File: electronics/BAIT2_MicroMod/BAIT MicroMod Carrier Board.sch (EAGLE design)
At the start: 113 parts, among them J1 JTAG, J11 microSD, J2 JTAG, J3 QWIIC_RIGHT_ANGLE, J4 JST_6_PIN_VERTICAL, J6 MICROMOD-2222-C, U1 3.3V, U2 S-1172B33-E6T1U, U3 LoRa-E5-HF, U5 3.3V, U6 BQ27441-G1, X1 2.1mm DC, X2 BQ24074

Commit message: Schematic V1 complete
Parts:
- added E5_EXTRA_PINS: (no value), SparkFun-Connectors:CONN_15
- added MICROMOD_EXTRA_PINS: (no value), SparkFun-Connectors:CONN_08"
- added POWER_PINS: (no value), SparkFun-Connectors:CONN_05
- added XB_EXTRA_PINS: (no value), SparkFun-Connectors:CONN_02
- C16: device SparkFun-Capacitors:1.0UF-16V-10%(0603) -> SparkFun-Capacitors:1.0UF-0603-16V-10%
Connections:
- removed net N$12: R1.1
- removed net N$23: U$7.DO8
- removed net N$24: U$7.RESET
- removed net N$26: U$7.PWM1
- removed net N$27: U$7.RESERVED
- removed net N$29: U$7.DTR/DI8
- removed net N$30: U$7.AD4/DIO4
- removed net N$31: U$7.CTS/DIO7
- removed net N$32: U$7.ON/SLEEP
- removed net N$33: U$7.VREF
- removed net N$35: U$7.RTS/AD6/DIO6
- removed net N$36: U$7.AD3/DIO3
- removed net N$37: U$7.AD2/DIO2
- removed net N$38: U$7.AD1/DIO1
- removed net N$39: U$7.AD0/DIO0
- removed net SCL: U6.SCL
- removed net SDA: U6.SDA
- removed net VLIPO: BATT1.2, C16.1, C2.1, C3.1, R24.2, U6.BAT, U6.SRP
- new net XB_ON: U$7.ON/SLEEP, XB_EXTRA_PINS.1
- new net XB_RST: U$7.RESET, XB_EXTRA_PINS.2
- net 3.3V: now also POWER_PINS.2
- net 3.3V_EN: now also MICROMOD_EXTRA_PINS.1
- net A0: now also MICROMOD_EXTRA_PINS.7
- net A1: now also MICROMOD_EXTRA_PINS.6
- net D0: now also MICROMOD_EXTRA_PINS.4
- net D1: now also MICROMOD_EXTRA_PINS.3
- net GND: now also POWER_PINS.1
- net HEADER_!CS!: now also MICROMOD_EXTRA_PINS.2
- net I2C_!INT!: now also MICROMOD_EXTRA_PINS.8
- net I2C_SCL: now also U6.SCL
- net I2C_SDA: now also U6.SDA
- net PA0/D0: now also E5_EXTRA_PINS.1
- net PA10/MOSI: now also E5_EXTRA_PINS.5
- net PA2/TX2: now also E5_EXTRA_PINS.13
- net PA3/RX2: now also E5_EXTRA_PINS.12
- net PA9/D9: now also E5_EXTRA_PINS.15
- net PB10/D10: now also E5_EXTRA_PINS.14
- net PB13/BOOT/SCK: now also E5_EXTRA_PINS.2
- net PB14/MISO: now also E5_EXTRA_PINS.4
- net PB3/A3: now also E5_EXTRA_PINS.6
- net PB4/A4: now also E5_EXTRA_PINS.7
- net PB5/LED: now also E5_EXTRA_PINS.8
- net PB9/NSS: now also E5_EXTRA_PINS.3
- net PC0/RX1: now also E5_EXTRA_PINS.10
- net PC1/TX1: now also E5_EXTRA_PINS.9
- net PWM0: now also R1.1
- net PWM1: now also MICROMOD_EXTRA_PINS.5
- net RST: now also E5_EXTRA_PINS.11
- net V+: now also POWER_PINS.4
- net VBUS: now also POWER_PINS.5
- net VIN: now also BATT1.2, C16.1, C2.1, C3.1, R24.2, U6.BAT, U6.SRP
- net V_BATT: now also POWER_PINS.3
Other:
- note added: "Headers"
- moved on the sheet: C17

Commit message: Initial board layout
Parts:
- removed 3V3_LED1, IN_LED, IN_LED1, OUT_LED, OUT_LED1, VIN_LED1: JUMPER-SMT_2_NC_TRACE_SILK, SparkFun-Jumpers:JUMPER-SMT_2_NC_TRACE_SILK
- removed BATT1: JST 2PH, adafruit:JST_2PIN-SMT-RA
- removed BT1: ML414H, SparkFun-Batteries:ML414H_IV01E_BATTERY
- removed C1, C16, C19: 1.0uF, SparkFun-Capacitors:1.0UF-0603-16V-10%
- removed C17: 0.47uF, SparkFun-Capacitors:CAP0603-CAP
- removed C18: 10uF, SparkFun-Capacitors:10UF-POLAR-EIA3216-16V-10%(TANT)
- removed C2: 10uF, microbuilder:CAP_CERAMIC0805-NOOUTLINE
- removed C20, C46, C9: 0.1uF, SparkFun-Capacitors:0.1UF-0603-25V-(+80/-20%)
- removed C21, C8: 0.22uF, SparkFun-Capacitors:0.22UF-0603-25V-10%
- removed D11, D3: GREEN, SparkFun-LED:LED-GREEN0603
- removed D13, D14, D5: RED, SparkFun-LED:LED-RED0603
- removed D2: BAS70-05, SparkFun-DiscreteSemi:DIODE-SCHOTTKY-DUAL
- removed D6: 3A/10V/280mV, SparkFun-DiscreteSemi:DIODE-SCHOTTKY-BAT60A
- removed D7: RED, microbuilder:LED0603
- removed D8: SK34A, microbuilder:DIODE-SCHOTTKYSMA
- removed D9: Yellow, SparkFun-LED:LED-YELLOW0603
- removed J11: microSD, SparkFun-Connectors:MICRO-SD-SDIOPUSH-PUSH
- removed J3: QWIIC_RIGHT_ANGLE, SparkFun-Connectors:QWIIC_CONNECTORJS-1MM
- removed J7: (no value), SparkFun-Connectors:CONN_02-JST-2MM-SMT
- removed JP2, JP4, JP6, JP7, JP8, JP9: JUMPER-SMT_3_1-NC_TRACE_SILK, SparkFun-Jumpers:JUMPER-SMT_3_1-NC_TRACE_SILK
- removed JP3: (no value), microbuilder:HEADER-1X1
- removed MEAS1: JUMPER-COMBO_2_NC_TRACE, SparkFun-Jumpers:JUMPER-COMBO_2_NC_TRACE
- removed R11, R19, R2, R6, R7: 1k, SparkFun-Resistors:1KOHM-0603-1/10W-1%
- removed R18: 590, microbuilder:RESISTOR_0603_NOOUT
- removed R20: 1K, microbuilder:RESISTOR_0603_NOOUT
- removed R22: 2.2k, SparkFun-Resistors:2.2KOHM-0603-1/10W-1%
- removed R25: 4.7k, SparkFun-Resistors:4.7KOHM-0603-1/10W-1%
- removed R26: 100k, SparkFun-Resistors:100KOHM-0603-1/10W-1%
- removed R27, R28, R29, R30: 10K, microbuilder:RESISTOR_0603_NOOUT
- removed R5: 3.3k, SparkFun-Resistors:3.3KOHM-0603-1/10W-1%
- removed THERM1: JUMPER-SMT_2_NO_NO-SILK, SparkFun-Jumpers:JUMPER-SMT_2_NO_NO-SILK
- removed U1: 3.3V, SparkFun-IC-Power:V_REG_AP2112K-3.3V
- removed U2: S-1172B33-E6T1U, Ablic:S-1172B33-E6T1U
- removed U6: BQ27441-G1, SparkFun-PowerIC:BQ27441-G1
- added 3V3_LED2, J_RX, J_TX, VIN_LED2: JUMPER-SMT_2_NC_TRACE_SILK, SparkFun-Jumpers:JUMPER-SMT_2_NC_TRACE_SILK
- added BATT2: JST 2PH, adafruit:JST_2PIN-SMT-RA
- added BT3: ML414H, SparkFun-Batteries:ML414H_IV01E_BATTERY
- added C13, C14, C28: 1.0uF, SparkFun-Capacitors:1.0UF-0603-16V-10%
- added C22: 10uF, microbuilder:CAP_CERAMIC0805-NOOUTLINE
- added C25, C30: 0.22uF, SparkFun-Capacitors:0.22UF-0603-25V-10%
- added C26, C29, C6: 0.1uF, SparkFun-Capacitors:0.1UF-0603-25V-(+80/-20%)
- added C27: 10uF, SparkFun-Capacitors:10UF-POLAR-EIA3216-16V-10%(TANT)
- added C7: 0.47uF, SparkFun-Capacitors:CAP0603-CAP
- added D16: Yellow, SparkFun-LED:LED-YELLOW0603
- added D17: RED, microbuilder:LED0603
- added D18: 3A/10V/280mV, SparkFun-DiscreteSemi:DIODE-SCHOTTKY-BAT60A
- added D19: BAS70-05, SparkFun-DiscreteSemi:DIODE-SCHOTTKY-DUAL
- added D20: SK34A, microbuilder:DIODE-SCHOTTKYSMA
- added D21: GREEN, microbuilder:LED0603
- added D_RX: GREEN, SparkFun-LED:LED-GREEN0603
- added D_TX: RED, SparkFun-LED:LED-RED0603
- added E5_SWO: JTAG, SparkFun-Connectors:CORTEX_JTAG_DEBUG_MINIMUM_PTH
- added JP_CIPO, JP_COPI, JP_CS, JP_SCK: JUMPER-SMT_3_1-NC_TRACE_SILK, SparkFun-Jumpers:JUMPER-SMT_3_1-NC_TRACE_SILK
- added LORA-E5: LoRa-E5-HF, moudle-new:MOUDLE_LORA_E5
- added MEAS2: JUMPER-COMBO_2_NC_TRACE, SparkFun-Jumpers:JUMPER-COMBO_2_NC_TRACE
- added QWIIC_PWR: JUMPER-SMT_3_2-NC_TRACE_SILK, SparkFun-Jumpers:JUMPER-SMT_3_2-NC_TRACE_SILK
- added R32: 3.3k, SparkFun-Resistors:3.3KOHM-0603-1/10W-1%
- added R34, R35: 2.2k, SparkFun-Resistors:2.2KOHM-0603-1/10W-1%
- added R36: 100k, SparkFun-Resistors:100KOHM-0603-1/10W-1%
- added R38, R41, R42, R43, R44: 10K, microbuilder:RESISTOR_0603_NOOUT
- added R39: 590, microbuilder:RESISTOR_0603_NOOUT
- added R40: 1K, microbuilder:RESISTOR_0603_NOOUT
- added REG1: S-1172B33-E6T1U, Ablic:S-1172B33-E6T1U
- added R_RX, R_TX: 1k, SparkFun-Resistors:1KOHM-0603-1/10W-1%
- added SOLAR_JST1: (no value), SparkFun-Connectors:CONN_02-JST-2MM-SMT
- added THERM2: JUMPER-SMT_2_NO_NO-SILK, SparkFun-Jumpers:JUMPER-SMT_2_NO_NO-SILK
- added U4: 3.3V, SparkFun-IC-Power:V_REG_AP2112K-3.3V
- added USBC: (no value), SparkFun-Connectors:USB_C_2-LAYER_PADS
- C15: value 1.0uF -> 10uF; device SparkFun-Capacitors:1.0UF-0603-16V-10% -> microbuilder:CAP_CERAMIC0805-NOOUTLINE
- C3: value 10uF -> 1.0uF; device microbuilder:CAP_CERAMIC0805-NOOUTLINE -> SparkFun-Capacitors:1.0UF-16V-10%(0603)
- D10: value GREEN -> RED; device microbuilder:LED0603 -> SparkFun-LED:LED-RED0603
- J1: value JTAG -> microSD; device SparkFun-Connectors:CORTEX_JTAG_DEBUG_MINIMUM_PTH -> SparkFun-Connectors:MICRO-SD-SDIOPUSH-PUSH
- J5: value (none) -> QWIIC_RIGHT_ANGLE; device SparkFun-Connectors:USB_C_2-LAYER_PADS -> SparkFun-Connectors:QWIIC_CONNECTORJS-1MM
- JP1: value JUMPER-SMT_3_2-NC_TRACE_SILK -> (none); device SparkFun-Jumpers:JUMPER-SMT_3_2-NC_TRACE_SILK -> microbuilder:HEADER-1X1
- R17: value 10K -> 0.01; device microbuilder:RESISTOR_0603_NOOUT -> SparkFun-Resistors:RESISTOR1206; PROD_ID (none) -> RES-13218
- R21: value 2.2k -> 100k; device SparkFun-Resistors:2.2KOHM-0603-1/10W-1% -> SparkFun-Resistors:100KOHM-0603-1/10W-1%
- R23: value 100k -> 1k; device SparkFun-Resistors:100KOHM-0603-1/10W-1% -> SparkFun-Resistors:1KOHM-0603-1/10W-1%
- R24: value 0.01 -> 4.7k; device SparkFun-Resistors:RESISTOR1206 -> SparkFun-Resistors:4.7KOHM-0603-1/10W-1%; PROD_ID RES-13218 -> (none)
- U3: value LoRa-E5-HF -> 3.3V; device moudle-new:MOUDLE_LORA_E5 -> SparkFun-IC-Power:V_REG_AP2112K-3.3V
- U5: value 3.3V -> BQ27441-G1; device SparkFun-IC-Power:V_REG_AP2112K-3.3V -> SparkFun-PowerIC:BQ27441-G1; PROD_ID (none) -> IC-13220
- renumbered ASC_LED to J_ASC, D12 to D_RSSI\, D4 to D_ASC, J2 to MM_SWO, J6 to MICROMOD, R4 to R_ASC, R8 to R_RSSI, RSSI_LED to J_RSSI, U$7 to XBEE
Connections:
- removed net N$11: R28.1, THERM1.1
- removed net N$14: BT1.+, D6.A, R5.1
- removed net N$15: JP1.3, R22.2
- removed net N$17: MEAS1.1, U2.VOUT
- removed net N$18: 3V3_LED1.1, R6.2
- removed net N$20: D5.A, R6.1
- removed net N$21: R25.2, VIN_LED1.1
- removed net N$22: D9.A, R25.1
- removed net N$40: IN_LED.1, R7.2
- removed net N$41: D11.A, R7.1
- removed net N$46: OUT_LED.1, R19.2
- removed net N$47: D14.A, R19.1
- removed net N$7: D7.C, R17.2
- removed net N$8: D10.C, R29.2
- removed net XB_IN: JP9.3, XBEE.DIN
- removed net XB_OUT: JP8.3, XBEE.DOUT
- new net GND1: SOLAR_JST1.2, X1.GND, X1.GNDBREAK
- new net N$23: BT3.+, D18.A, R32.1
- new net N$24: QWIIC_PWR.3, R35.2
- new net N$26: QWIIC_PWR.1, R34.2
- new net N$27: D10.A, R23.1
- new net N$29: R24.2, VIN_LED2.1
- new net N$30: D20.A, SOLAR_JST1.1, X1.PWR
- new net N$31: D17.C, R38.2
- new net N$32: D21.C, R43.2
- new net N$33: R42.1, THERM2.1
- new net N$37: D16.A, R24.1
- new net OUT: X2.EN2
- new net V+1: REG1.VIN
- net !CE: now also R44.1; no longer R30.1
- net !CHG: now also R38.1; no longer R17.1
- net !PGOOD: now also R43.1; no longer R29.1
- net 1.8V: now also C7.1, U5.VDD; no longer C17.1, U6.VDD
- net 3.3V: now also 3V3_LED2.2, C28.1, C29.1, C30.1, D19.A1, E5_SWO.VCC, J_RX.2, J_TX.2, LORA-E5.VCC, MEAS2.2, R21.2, R36.2; no longer 3V3_LED1.2, C19.1, C20.1, C21.1, D2.A1, IN_LED.2, IN_LED1.2, J1.VCC, MEAS1.2, OUT_LED.2, OUT_LED1.2, R23.2, R26.2, U3.VCC
- net 3.3V_LP: now also C14.1, C6.1, J1.VCC, U4.OUT; no longer C1.1, C46.1, J11.VCC, U1.OUT
- net CLK/SCK: now also J1.CLK/SCK, JP_SCK.3; no longer J11.CLK/SCK, JP6.3
- net CMD/CIPO: now also J1.CMD/SDI, JP_CIPO.3; no longer J11.CMD/SDI, JP7.3
- net DAT0/COPI: now also J1.DAT0/SDO, JP_COPI.3; no longer J11.DAT0/SDO, JP4.3
- net DAT3/!CS!: now also J1.DAT3/!CS!, JP_CS.3; no longer J11.DAT3/!CS!, JP2.3
- net GND: now also BATT2.1, BT3.-, C13.2, C14.2, C22.2, C25.2, C26.2, C27.-, C28.2, C29.2, C30.2, C6.2, C7.2, D10.C, D16.C, E5_SWO.GND, J1.SHIELD, J5.1, JP1.1, LORA-E5.GND, LORA-E5.GND@1, LORA-E5.GND@2, LORA-E5.GND@3, R39.2, R40.2, R41.2, R42.2, R44.2, REG1.VSS, REG1.VSS_2, U4.GND, U5.PWPD, U5.VSS, USBC.GND; no longer BATT1.1, BT1.-, C1.2, C16.2, C17.2, C18.-, C19.2, C2.2, C20.2, C21.2, C46.2, C8.2, C9.2, D5.C, D9.C, J11.GND, J11.SHIELD, J3.1, J5.GND, J7.2, JP3.1, R18.2, R20.2, R27.2, R28.2, R30.2, U1.GND, U2.VSS, U2.VSS_2, U3.GND@1, U3.GND@2, U3.GND@3, U5.GND, U6.PWPD, U6.VSS, X1.GND, X1.GNDBREAK
- net GPOUT: now also U5.GPOUT; no longer U6.GPOUT
- net I2C_SCL: now also J5.4, R35.1, U5.SCL; no longer J3.4, R22.1, U6.SCL
- net I2C_SDA: now also J5.3, R34.1, U5.SDA; no longer J3.3, R21.1, U6.SDA
- net ILIM: now also R40.1; no longer R20.1
- net ISET: now also R39.1; no longer R18.1
- net ITERM: now also R41.1; no longer R27.1
- net N$16: now also 3V3_LED2.1, R23.2; no longer JP1.1, R21.2
- net N$19: now also LORA-E5.VDD_TCXO; no longer U3.VDD_TCXO
- net N$3: now also J_RX.1, R_RX.2; no longer IN_LED1.1, R2.2
- net N$4: now also USBC.CC1; no longer J5.CC1
- net N$44: now also J_TX.1, R_TX.2; no longer OUT_LED1.1, R11.2
- net N$45: now also D_TX.A, R_TX.1; no longer D13.A, R11.1
- net N$48: now also USBC.VBUS; no longer J5.VBUS
- net N$5: now also USBC.CC2; no longer J5.CC2
- net N$6: now also MEAS2.1, REG1.VOUT; no longer D8.A, J7.1, X1.PWR
- net N$9: now also D_RX.A, R_RX.1; no longer D3.A, R2.1
- net PA0/D0: now also LORA-E5.PA0; no longer U3.PA0
- net PA10/MOSI: now also LORA-E5.PA10; no longer U3.PA10
- net PA13/SWDIO: now also E5_SWO.SWDIO, LORA-E5.PA13; no longer J1.SWDIO, U3.PA13
- net PA14/SWCLK: now also E5_SWO.SWDCLK, LORA-E5.PA14; no longer J1.SWDCLK, U3.PA14
- net PA15/SDA: now also LORA-E5.PA15; no longer U3.PA15
- net PA2/TX2: now also LORA-E5.PA2; no longer U3.PA2
- net PA3/RX2: now also LORA-E5.PA3; no longer U3.PA3
- net PA9/D9: now also LORA-E5.PA9; no longer U3.PA9
- net PB10/D10: now also LORA-E5.PB10; no longer U3.PB10
- net PB13/BOOT/SCK: now also LORA-E5.PB13; no longer U3.PB13
- net PB14/MISO: now also LORA-E5.PB14; no longer U3.PB14
- net PB15/SCL: now also LORA-E5.PB15; no longer U3.PB15
- net PB3/A3: now also LORA-E5.PB3; no longer U3.PB3
- net PB4/A4: now also LORA-E5.PB4; no longer U3.PB4
- net PB5/LED: now also LORA-E5.PB5; no longer U3.PB5
- net PB9/NSS: now also LORA-E5.PB9; no longer U3.PB9
- net PC0/RX1: now also LORA-E5.PC0; no longer U3.PC0
- net PC1/TX1: now also LORA-E5.PC1; no longer U3.PC1
- net PERIPHERAL_PWR_CTRL: now also R21.1, U4.EN; no longer R26.1, U1.EN
- net QWIIC_PWR: now also C13.1, J5.2, QWIIC_PWR.2, U3.OUT; no longer C15.1, J3.2, JP1.2, U5.OUT
- net QWIIC_PWR_CTRL: now also R36.1, U3.EN; no longer R23.1, U5.EN
- net RF: now also LORA-E5.RFI0; no longer U3.RFI0
- net RST: now also E5_SWO.!RESET, LORA-E5.RST; no longer J1.!RESET, U3.RST
- net RTC_3V: now also D18.C, D19.C, R32.2; no longer D2.C, D6.C, R5.2
- net RX: now also D_RX.C, LORA-E5.PB7, XBEE.DOUT; no longer D3.C, JP8.2, U3.PB7
- net RX2: no longer D11.C, JP8.1
- net SD_!CS!: now also JP_CS.1; no longer JP2.1
- net SD_CLK: now also JP_SCK.2; no longer JP6.2
- net SD_CMD: now also JP_CIPO.2; no longer JP7.2
- net SD_DATA0: now also JP_COPI.2; no longer JP4.2
- net SD_DATA1: now also J1.DAT1/NC; no longer J11.DAT1/NC
- net SD_DATA2: now also J1.DAT2/NC; no longer J11.DAT2/NC
- net SD_DATA3: now also JP_CS.2; no longer JP2.2
- net SPI_CIPO: now also JP_CIPO.1; no longer JP7.1
- net SPI_COPI: now also JP_COPI.1; no longer JP4.1
- net SPI_SCK: now also JP_SCK.1; no longer JP6.1
- net THERM: now also THERM2.2; no longer THERM1.2
- net TS: now also U5.BIN; no longer U6.BIN
- net TX: now also D_TX.C, LORA-E5.PB6, XBEE.DIN; no longer D13.C, JP9.2, U3.PB6
- net TX2: no longer D14.C, JP9.1
- net USB_D+: now also USBC.D+; no longer J5.D+
- net USB_D-: now also USBC.D-; no longer J5.D-
- net V+: now also C25.1, C26.1, C27.+, D17.A, D21.A, U3.IN, U4.IN, VIN_LED2.2; no longer C18.+, C8.1, C9.1, D10.A, D7.A, U1.IN, U2.VIN, VIN_LED1.2, X2.EN2
- net VBUS: now also D20.C; no longer D8.C
- net VIN: now also BATT2.2, C15.1, C22.1, R17.2, U5.BAT, U5.SRP; no longer BATT1.2, C16.1, C2.1, R24.2, U5.IN, U6.BAT, U6.SRP
- net V_BATT: now also R17.1, U5.SRN; no longer R24.1, U6.SRN
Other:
- note added: "Close VE to enable processor control of 3.3V bus."
- note removed: "BQ27441-G1 Fuel Gauge"
- note removed: "Closing jumper bypasses PTC to allow >2A current flows."
- note removed: "External Capacitor"
- note removed: "LiPo Solar Charger"
- note removed: "Peripheral Power Control"
- note removed: "Qwiic"
- note removed: "RTC"
- note removed: "USB"
- note removed: "Voltage Regulation"

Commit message: Board layout updates
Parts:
- removed ANT1: DIP SMA-K, Connector-new:ANTENNA-SMA-MCX-JE-320160125
- removed R16: DNP, Discrete-new:RES-0402
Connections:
- removed net N$10: ANT2.D, R16.2
- removed net N$13: ANT1.ANT, R15.2
- new net N$7: ANT2.D, R15.2
- net GND: no longer ANT1.2, ANT1.3, ANT1.4, ANT1.5
- net N$28: no longer R16.1
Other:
- moved on the sheet: ANT2, C11, C12, R14, R15

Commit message: Files for First Prototype production
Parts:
- removed 3V3_LED2: JUMPER-SMT_2_NC_TRACE_SILK, SparkFun-Jumpers:JUMPER-SMT_2_NC_TRACE_SILK
- removed BATT2: JST 2PH, adafruit:JST_2PIN-SMT-RA
- removed BT3: ML414H, SparkFun-Batteries:ML414H_IV01E_BATTERY
- removed D_ASC, D_RSSI\, D_RX: GREEN, SparkFun-LED:LED-GREEN0603
- removed D_TX: RED, SparkFun-LED:LED-RED0603
- removed LORA-E5: LoRa-E5-HF, moudle-new:MOUDLE_LORA_E5
- removed MICROMOD: MICROMOD-2222-C, SparkFun-MicroMod:MICROMOD-2222-C
- removed REG1: S-1172B33-E6T1U, Ablic:S-1172B33-E6T1U
- removed R_ASC: 4.7k, SparkFun-Resistors:4.7KOHM-0603-1/10W-1%
- removed R_RSSI, R_RX, R_TX: 1k, SparkFun-Resistors:1KOHM-0603-1/10W-1%
- removed S1: Reset, SparkFun-Switches:MOMENTARY-SWITCH-SPST-SMD-5.2-TALL-REDUNDANT
- removed S2: BOOT, SparkFun-Switches:MOMENTARY-SWITCH-SPST-SMD-5.2-TALL-REDUNDANT
- removed SOLAR_JST1: (no value), SparkFun-Connectors:CONN_02-JST-2MM-SMT
- removed USBC: (no value), SparkFun-Connectors:USB_C_2-LAYER_PADS
- removed X1: 2.1mm DC, microbuilder:DCBARRELSMT
- removed X2: BQ24074, adafruit_power:BQ24074
- removed XBEE: XBEE, adafruit:XBEE
- added 3V3_LED, GND_CON: JUMPER-SMT_2_NC_TRACE_SILK, SparkFun-Jumpers:JUMPER-SMT_2_NC_TRACE_SILK
- added ANT1: 0868AT43A0020EANT_0868AT43A0020E_JOT, 2023-01-04_20-35-52_Library:0868AT43A0020EANT_0868AT43A0020E_JOT
- added BT1: ML414H, SparkFun-Batteries:ML414H_IV01E_BATTERY
- added C1, C17, C19, C20, C21, C23, C31, C8: 2.2uF, SparkFun-Capacitors:10UF-POLAR-0603-6.3V-20%(TANT)
- added C16, C2, C24, C9: 0.1uF, SparkFun-Capacitors:10UF-POLAR-EIA3216-16V-10%(TANT)
- added C18: 0.15uF, SparkFun-Capacitors:10UF-POLAR-EIA3216-16V-10%(TANT)
- added C32, C34, C35, C37, C38: 100nf, OPL_Capacitor:CERAMIC-100NF-50V-10%-X7R(0603)
- added C33: 4.7uF, Discrete-new:CAP-0603
- added C36: 10uf, OPL_Capacitor:TANTALUM-SMD-10UF-16V-10%(AVX-A)
- added C39: 220pF, Capacitor:C_CHIP-0603(1608-METRIC)
- added D2, D3, D4: GREEN, SparkFun-LED:LED-GREEN0603
- added D5: RED, SparkFun-LED:LED-RED0603
- added F1: 6V/2A, Circuit-Protection:FUSE_CHIP-1206(3216-METRIC)
- added FB1: 600Ω/1.8A, SparkFun-Coils:FERRITE_BEAD-0603
- added J10: QWIIC_RIGHT_ANGLE, SM04B-SRSS-TB_LF__SN_:SM04B-SRSS-TB(LF)(SN)
- added J15: SM06B-SRSS-TB(LF)(SN), SM06B-SRSS-TB_LF__SN_:SM06B-SRSS-TB(LF)(SN)
- added J2: ST-TF-003A, ST-TF-003A:ST-TF-003A
- added J3: (no value), SparkFun-RF:XBEESMD
- added J6: JST 2PH, adafruit:JST_2PIN-SMT-RA
- added J7: MICROMOD-2222-C, SparkFun-MicroMod:MICROMOD-2222-C
- added J8: (no value), SparkFun-Connectors:CONN_02-JST-2MM-SMT
- added J9: (no value), SparkFun-Connectors:USB_C_2-LAYER_PADS
- added LINEIN, LINEOUT: (no value), SparkFun-Connectors:CONN_03
- added MIC_3V3, MIC_GND: JUMPER-SMT_3_2-NC_TRACE_SILK, SparkFun-Jumpers:JUMPER-SMT_3_2-NC_TRACE_SILK
- added MK1: ICS-43432, Audio-Devices:ICS-43432
- added MK1_LR: MK1_LR, SparkFun-Jumpers:JUMPER-SMT_3_1-NC_TRACE_SILK
- added MK2: SPH0645LM4H-B, SPH0645LM4H-B:SPH0645LM4H-B
- added MK2_LR: MK2_LR, SparkFun-Jumpers:JUMPER-SMT_3_1-NC_TRACE_SILK
- added R11, R5: 4.7K, OPL_Resistor:SMD-RES-4.7K-5%-1/10W(0603)
- added R18: 100K, OPL_Resistor:SMD-RES-100K-1%-1/10W(0603)
- added R2: 2.2K, OPL_Resistor:SMD-RES-2.2K-5%-1/10W(0603)
- added R4: 0R, OPL_Resistor:SMD-RES-0R-5%-1/10W(0603)
- added R6, R7, R8: 1K 1/10W, OPL_Resistor:SMD-RES-1K-5%-1/10W(0603)
- added SW1, SW2: SKQGADE010, OPL_Switch:SMD-BUTTON(4P-5.2X5.2X1.5MM-SKQGADE010)-SKQGADE010
- added TP1, TP3: PTR1TP06R, testpad:PTR1TP06R
- added U1: SGTL5000-32, Freescale:SGTL5000-32
- added U10: TSL25911, 2023-02-07_20-42-29_Library:TSL25911FNSON-06-FN_2000X2400_AMS
- added U2: AP7313, 2022-08-05_10-01-44_Library:AP7313
- added U6: BQ24074, adafruit_power:BQ24074
- added U7: LoRa-E5-HF, moudle-new:MOUDLE_LORA_E5
- added U8: S-1172B33-E6T1U, Ablic:S-1172B33-E6T1U
- added U9: BOSCH_TOOLS_BME680BOSCH_TOOLS_BME680_0_0, Bosch Tools - BME680:BOSCH_TOOLS_BME680BOSCH_TOOLS_BME680_0_0
- C10: value 4.7uF -> 4.7uf; device Discrete-new:CAP-0603 -> OPL_Capacitor:CERAMIC-4.7UF-10V-10%-X5R(0603)
- C13, C14, C28: value 1.0uF -> 1uf; device SparkFun-Capacitors:1.0UF-0603-16V-10% -> OPL_Capacitor:CERAMIC-1UF-25V-10%-X7R(0603)
- C15, C22, C4, C5: value 10uF -> 4.7uf; device microbuilder:CAP_CERAMIC0805-NOOUTLINE -> OPL_Capacitor:CERAMIC-4.7UF-10V-10%-X5R(0603)
- C25, C30: value 0.22uF -> 220nf; device SparkFun-Capacitors:0.22UF-0603-25V-10% -> OPL_Capacitor:CERAMIC-220NF-25V-10%-X7R(0603)
- C26, C29, C6: value 0.1uF -> 100nf; device SparkFun-Capacitors:0.1UF-0603-25V-(+80/-20%) -> OPL_Capacitor:CERAMIC-100NF-50V-10%-X7R(0603)
- C27: value 10uF -> 10uf; device SparkFun-Capacitors:10UF-POLAR-EIA3216-16V-10%(TANT) -> OPL_Capacitor:TANTALUM-SMD-10UF-16V-10%(AVX-A)
- C3: value 1.0uF -> 1uf; device SparkFun-Capacitors:1.0UF-16V-10%(0603) -> OPL_Capacitor:CERAMIC-1UF-25V-10%-X7R(0603)
- C7: MPN (none) -> TACL474K010XTA
- D1: MPN (none) -> BAS16J,115
- D15, D20: MPN (none) -> SK34A-LTP
- D16: MPN (none) -> LTST-S270KSKT
- D17: device microbuilder:LED0603 -> SparkFun-LED:LED-RED0603
- D18: MPN (none) -> BAT60AE6327HTSA1
- D19: MPN (none) -> BAS70-05-7-F
- D21: device microbuilder:LED0603 -> SparkFun-LED:LED-GREEN0603
- J1: value microSD -> SJ-43516-SMT; device SparkFun-Connectors:MICRO-SD-SDIOPUSH-PUSH -> SnapEDA-Library:SJ-43516-SMT; MPN (none) -> SJ-43516-SMT
- J4: MPN (none) -> BM06B-SRSS-TB(LF)(SN)
- J5: MPN (none) -> BM04B-SRSS-TB(LF)(SN)
- LS1: MPN (none) -> 102-CMT-7525-80-SMT-TR-ND
- R1: value 180 -> 200K; device SparkFun-Resistors:180OHM-0603-1/10W-1% -> OPL_Resistor:SMD-RES-200K-5%-1/10W(0603)
- R10: value 20k -> 20K; device SparkFun-Resistors:20KOHM-0603-1/10W-1% -> OPL_Resistor:SMD-RES-20K-1%-1/10W(0603)
- R14, R15: device Discrete-new:RES-0402 -> OPL_Resistor:SMD-RES-0R-5%-1/10W(0603)
- R17: MPN (none) -> LR1206-21R010J4
- R21, R3, R36: value 100k -> 100K; device SparkFun-Resistors:100KOHM-0603-1/10W-1% -> OPL_Resistor:SMD-RES-100K-1%-1/10W(0603)
- R23: value 1k -> 1K 1/10W; device SparkFun-Resistors:1KOHM-0603-1/10W-1% -> OPL_Resistor:SMD-RES-1K-5%-1/10W(0603)
- R24: value 4.7k -> 4.7K; device SparkFun-Resistors:4.7KOHM-0603-1/10W-1% -> OPL_Resistor:SMD-RES-4.7K-5%-1/10W(0603)
- R32: value 3.3k -> 3.3K; device SparkFun-Resistors:3.3KOHM-0603-1/10W-1% -> OPL_Resistor:SMD-RES-3.3K-1%-1/10W(0603)
- R34, R35: value 2.2k -> 2.2K; device SparkFun-Resistors:2.2KOHM-0603-1/10W-1% -> OPL_Resistor:SMD-RES-2.2K-5%-1/10W(0603)
- R38, R41, R42, R43, R44: value 10K -> 10K 1/10W; device microbuilder:RESISTOR_0603_NOOUT -> OPL_Resistor:SMD-RES-10K-5%-1/10W(0603)
- R39: device microbuilder:RESISTOR_0603_NOOUT -> OPL_Resistor:SMD-RES-560R-5%-1/10W(0603); MPN (none) -> RC0603FR-07590RL
- R40: value 1K -> 1K 1/10W; device microbuilder:RESISTOR_0603_NOOUT -> OPL_Resistor:SMD-RES-1K-5%-1/10W(0603)
- R9: value 10k -> 10K 1/10W; device SparkFun-Resistors:10KOHM-0603-1/10W-1% -> OPL_Resistor:SMD-RES-10K-5%-1/10W(0603)
- TH1, TH2, TH3, TH4: device varistor:VARISTORCN0603 -> NTCG163JX103DT1S:NTCG163JX103DT1S
- TR1: MPN (none) -> MMBT2222ATPMSTR-ND
- U4: MPN (none) -> AP2112K-3.3TRG1
- U5: MPN (none) -> BQ27441DRZT-G1A
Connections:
- removed net GND1: SOLAR_JST1.2, X1.GND, X1.GNDBREAK
- removed net OUT: X2.EN2
- removed net PA15/SDA: LORA-E5.PA15
- removed net PB15/SCL: LORA-E5.PB15
- removed net RX2: MICROMOD.RX2
- removed net THERM: TH1.1, TH3.1, THERM2.2, X2.TS
- removed net TX2: MICROMOD.TX2
- removed net V+1: REG1.VIN
- removed net VCC: XBEE.VCC
- new net 3V3_B: C34.1, C35.1, J10.2, J15.1, MIC_3V3.2, MK1_LR.1, MK2_LR.3, TP1.TP, U10.VDD, U9.VDD
- new net 3V3_ICS: C37.1, MIC_3V3.3, MK1.VDD
- new net 3V3_SPH: C38.1, C39.1, MIC_3V3.1, MK2.VDD
- new net AGND: C18.-, GND_CON.1, LINEIN.1, LINEOUT.1, U1.AGND, U1.GND@1, U1.GND@2
- new net GND_B: C32.2, C34.2, C35.2, J10.1, J10.SHIELD, J15.2, J15.SHIELD, MIC_GND.2, MK1_LR.3, MK2_LR.1, R18.1, TP3.TP, U10.GND, U9.1_GND, U9.2_GND, U9.SDO
- new net GND_ICS: C37.2, MIC_GND.3, MK1.CONFIG, MK1.GND
- new net GND_SPH: C38.2, C39.2, MIC_GND.1, MK2.GND
- new net INT_B: U10.INT
- new net N$11: ANT1.1, R4.2
- new net N$13: C19.-, LINEOUT.3
- new net N$14: C20.-, LINEOUT.2
- new net N$15: C21.-, LINEIN.3
- new net N$17: C23.-, LINEIN.2
- new net N$18: C19.+, U1.LINEOUT_R
- new net N$20: C20.+, U1.LINEOUT_L
- new net N$21: C21.+, U1.LINEIN_R
- new net N$22: C23.+, U1.LINEIN_L
- new net N$33: C24.-, J1.SLEEVE, R2.2
- new net N$35: J1.RING1, U1.HP_R
- new net N$36: F1.1, J9.VBUS
- new net N$38: C18.+, U1.VAG
- new net N$39: C31.+, R2.1, U1.MIC_BIAS
- new net N$40: C24.+, U1.MIC
- new net N$41: C8.+, U1.DVDD, U2.OUT
- new net N$46: C1.+, C2.+, FB1.2, U1.AVDD
- new net N$54: C32.1, R11.2, U9.VDDIO
- new net N$55: R11.1, U9.!CS!
- new net N$8: J1.TIP, U1.HP_L
- new net SCK_B: J15.3, MK1.SCK, MK2.BCLK
- new net SCL_B: J10.4, U10.SCL, U9.SCK
- new net SDA_B: J10.3, U10.SDA, U9.SDI
- new net SD_B: J15.4, MK1.SD, MK2.DATA_OUT, R18.2
- new net SEL_MK1: MK1.LR, MK1_LR.2
- new net SEL_MK2: MK2.SELECT, MK2_LR.2
- new net USB_VIN: D15.A, F1.2, J7.USB_VIN
- new net WS_B: J15.5, MK1.WS, MK2.WS
- net !BOOT!: now also J7.!BOOT!, SW2.A1; no longer MICROMOD.!BOOT!, S2.2
- net !CE: now also U6.!CE; no longer X2.!CE
- net !CHG: now also U6.!CHG; no longer X2.!CHG
- net !PGOOD: now also U6.!PGOOD; no longer X2.!PGOOD
- net !RESET!: now also J7.!RESET!, SW1.A1; no longer MICROMOD.!RESET!, S1.2
- net 3.3V: now also 3V3_LED.2, C16.+, C17.+, C33.2, C36.+, C9.+, FB1.1, J3.VDD, J7.3.3V, J_RX.1, U1.VDDIO, U2.IN, U7.VCC; no longer 3V3_LED2.2, J_RX.2, LORA-E5.VCC, MICROMOD.3.3V
- net 3.3V_EN: now also J7.3.3V_EN; no longer MICROMOD.3.3V_EN
- net 3.3V_LP: now also J2.VDD; no longer J1.VCC
- net A0: now also J7.A0; no longer MICROMOD.A0
- net A1: now also J7.A1; no longer MICROMOD.A1
- net ASC: now also J3.DIO5; no longer XBEE.ASC/AD5/DIO5
- net CLK/SCK: now also J2.CLK, JP_SCK.2; no longer J1.CLK/SCK, JP_SCK.3
- net CMD/CIPO: now also J2.CMD, JP_CIPO.2; no longer J1.CMD/SDI, JP_CIPO.3
- net D0: now also J7.D0; no longer MICROMOD.D0
- net D1: now also J7.D1/CAM_TRIG; no longer MICROMOD.D1/CAM_TRIG
- net DAT0/COPI: now also J2.DAT0, JP_COPI.2; no longer J1.DAT0/SDO, JP_COPI.3
- net DAT3/!CS!: now also J2.DAT3, JP_CS.2; no longer J1.DAT3/!CS!, JP_CS.3
- net GND: now also BT1.-, C1.-, C16.-, C17.-, C2.-, C31.-, C33.1, C36.-, C8.-, C9.-, D2.C, D3.C, GND_CON.2, J2.GND, J2.VSS, J3.GND, J6.1, J7.GND, J8.2, J9.GND, SW1.B1, SW2.B1, U1.CTRL_ADR0_CS, U1.CTRL_MODE, U1.GND@PAD, U2.GND, U6.EN1, U6.TMR, U6.VSS, U7.GND, U7.GND@1, U7.GND@2, U7.GND@3, U8.VSS, U8.VSS_2; no longer BATT2.1, BT3.-, D_ASC.C, D_RSSI\.C, J1.GND, J1.SHIELD, LORA-E5.GND, LORA-E5.GND@1, LORA-E5.GND@2, LORA-E5.GND@3, MICROMOD.GND, REG1.VSS, REG1.VSS_2, S1.1, S2.1, USBC.GND, X2.EN1, X2.TMR, X2.VSS, XBEE.GND
- net GPOUT: now also J7.G6/BUS6
- net HEADER_!CS!: now also J7.G0/BUS0; no longer MICROMOD.G0/BUS0
- net I2C_!INT!: now also J7.I2C_!INT!; no longer MICROMOD.I2C_!INT!
- net I2C_SCL: now also J7.I2C_SCL, U1.CTRL_CLK; no longer MICROMOD.I2C_SCL
- net I2C_SDA: now also J7.I2C_SDA, U1.CTRL_DATA; no longer MICROMOD.I2C_SDA
- net I2S_SCK: now also J7.AUD_BCLK; no longer MICROMOD.AUD_BCLK
- net I2S_SD: now also J7.AUD_IN/CAM_PCLK; no longer MICROMOD.AUD_IN/CAM_PCLK
- net I2S_WS: now also J7.AUD_LRCLK; no longer MICROMOD.AUD_LRCLK
- net ILIM: now also U6.ILIM; no longer X2.ILIM
- net ISET: now also U6.ISET; no longer X2.ISET
- net ITERM: now also U6.ITERM; no longer X2.ITERM
- net LR_SEL: now also J7.G5/BUS5; no longer MICROMOD.G5/BUS5
- net N$16: now also 3V3_LED.1; no longer 3V3_LED2.1
- net N$19: now also U7.VDD_TCXO; no longer LORA-E5.VDD_TCXO
- net N$23: now also BT1.+; no longer BT3.+
- net N$25: now also R5.2; no longer R_ASC.2
- net N$28: now also R4.1
- net N$3: now also J_RX.2, R7.2; no longer J_RX.1, R_RX.2
- net N$30: now also J8.1; no longer SOLAR_JST1.1, X1.PWR
- net N$34: now also D2.A, R5.1; no longer D_ASC.A, R_ASC.1
- net N$4: now also J9.CC1; no longer USBC.CC1
- net N$42: now also R6.2; no longer R_RSSI.2
- net N$43: now also D3.A, R6.1; no longer D_RSSI\.A, R_RSSI.1
- net N$44: now also R8.2; no longer R_TX.2
- net N$45: now also D5.A, R8.1; no longer D_TX.A, R_TX.1
- net N$48: now also J1.RING2, U1.HP_VGND; no longer D15.A, USBC.VBUS
- net N$5: now also J9.CC2; no longer USBC.CC2
- net N$6: now also U8.VOUT; no longer REG1.VOUT
- net N$9: now also D4.A, R7.1; no longer D_RX.A, R_RX.1
- net PA0/D0: now also U7.PA0; no longer LORA-E5.PA0
- net PA10/MOSI: now also U7.PA10; no longer LORA-E5.PA10
- net PA13/SWDIO: now also U7.PA13; no longer LORA-E5.PA13
- net PA14/SWCLK: now also U7.PA14; no longer LORA-E5.PA14
- net PA2/TX2: now also U7.PA2; no longer LORA-E5.PA2
- net PA3/RX2: now also E5_EXTRA_PINS.14, U7.PA3; no longer E5_EXTRA_PINS.12, LORA-E5.PA3
- net PA9/D9: now also E5_EXTRA_PINS.11, U7.PA9; no longer E5_EXTRA_PINS.15, LORA-E5.PA9
- net PB10/D10: now also E5_EXTRA_PINS.12, U7.PB10; no longer E5_EXTRA_PINS.14, LORA-E5.PB10
- net PB13/BOOT/SCK: now also U7.PB13; no longer LORA-E5.PB13
- net PB14/MISO: now also U7.PB14; no longer LORA-E5.PB14
- net PB3/A3: now also U7.PB3; no longer LORA-E5.PB3
- net PB4/A4: now also U7.PB4; no longer LORA-E5.PB4
- net PB5/LED: now also E5_EXTRA_PINS.10, U7.PB5; no longer E5_EXTRA_PINS.8, LORA-E5.PB5
- net PB9/NSS: now also U7.PB9; no longer LORA-E5.PB9
- net PC0/RX1: now also E5_EXTRA_PINS.8, U7.PC0; no longer E5_EXTRA_PINS.10, LORA-E5.PC0
- net PC1/TX1: now also U7.PC1; no longer LORA-E5.PC1
- net PERIPHERAL_PWR_CTRL: now also J7.G1/BUS1; no longer MICROMOD.G1/BUS1
- net PWM0: now also J7.PWM0; no longer MICROMOD.PWM0
- net PWM1: now also J7.PWM1; no longer MICROMOD.PWM1
- net QWIIC_PWR_CTRL: now also J7.G2/BUS2; no longer MICROMOD.G2/BUS2
- net RF: now also U7.RFI0; no longer LORA-E5.RFI0
- net RSSI: now also J3.RSSI; no longer XBEE.PWM0/RSSI
- net RST: now also E5_EXTRA_PINS.15, U7.RST; no longer E5_EXTRA_PINS.11, LORA-E5.RST
- net RTC_3V: now also J7.RTC_3V; no longer MICROMOD.RTC_3V
- net RX: now also D4.C, J3.DOUT, J7.RX1, U7.PB7; no longer D_RX.C, LORA-E5.PB7, MICROMOD.RX1, XBEE.DOUT
- net SD_!CS!: now also J7.SPI_!CS!; no longer MICROMOD.SPI_!CS!
- net SD_CLK: now also J7.SPI_SCK1/SDIO_CLK, JP_SCK.3; no longer JP_SCK.2, MICROMOD.SPI_SCK1/SDIO_CLK
- net SD_CMD: now also J7.SPI_SDO1/SDIO_CMD, JP_CIPO.3; no longer JP_CIPO.2, MICROMOD.SPI_SDO1/SDIO_CMD
- net SD_DATA0: now also J7.SPI_SDI1/SDIO_DATA0, JP_COPI.3; no longer JP_COPI.2, MICROMOD.SPI_SDI1/SDIO_DATA0
- net SD_DATA1: now also J2.DAT1, J7.SDIO_DATA1; no longer J1.DAT1/NC, MICROMOD.SDIO_DATA1
- net SD_DATA2: now also J2.DAT2, J7.SDIO_DATA2; no longer J1.DAT2/NC, MICROMOD.SDIO_DATA2
- net SD_DATA3: now also J7.SPI_!CS1!/SDIO_DATA3, JP_CS.3; no longer JP_CS.2, MICROMOD.SPI_!CS1!/SDIO_DATA3
- net SPI_CIPO: now also J7.SPI_SDI; no longer MICROMOD.SPI_SDI
- net SPI_COPI: now also J7.SPI_SDO; no longer MICROMOD.SPI_SDO
- net SPI_SCK: now also J7.SPI_SCK; no longer MICROMOD.SPI_SCK
- net SWDCK: now also J7.SWDCK; no longer MICROMOD.SWDCK
- net SWDIO: now also J7.SWDIO; no longer MICROMOD.SWDIO
- net TS: now also TH1.1, TH3.1, THERM2.2, U6.TS
- net TX: now also D5.C, J3.DIN, J7.TX1, U7.PB6; no longer D_TX.C, LORA-E5.PB6, MICROMOD.TX1, XBEE.DIN
- net USB_D+: now also J7.USB_D+, J9.D+; no longer MICROMOD.USB_D+, USBC.D+
- net USB_D-: now also J7.USB_D-, J9.D-; no longer MICROMOD.USB_D-, USBC.D-
- net V+: now also U6.EN2, U6.OUT, U8.VIN; no longer X2.OUT
- net VBUS: now also U6.IN; no longer X2.IN
- net VIN: now also J6.2; no longer BATT2.2, MICROMOD.USB_VIN
- net VIN/3: now also J7.BATT_VIN/3; no longer MICROMOD.BATT_VIN/3
- net V_BATT: now also U6.BAT; no longer X2.BAT
- net XB_ON: now also J3.DIO9; no longer XBEE.ON/SLEEP
- net XB_RST: now also J3.RESET; no longer XBEE.RESET
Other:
- note added: "AGND (pin 7) should be "star" connected to the jack grounds for LINEIN and LINEOUT, and to the VAG capacitor ground. This node should via to the ground plane (or connected to ground) at a single point."
- note added: "Could be a problem that the micromod pinout uses different pins for SDIO than teensy does."
- moved on the sheet: ANT2, C11, C12, C7, D1, D10, D15, D16, D18, D19, D20, E5_EXTRA_PINS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

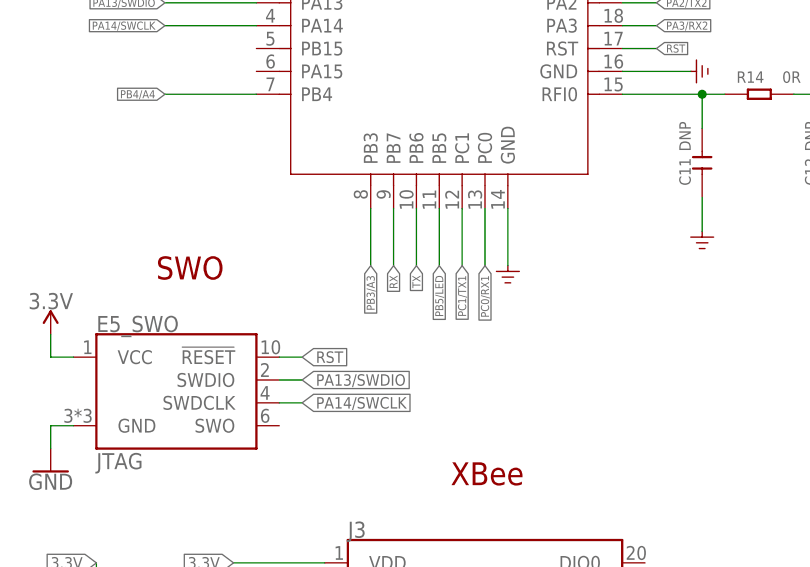
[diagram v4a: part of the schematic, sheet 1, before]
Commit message: Schematic fix for faulty connection between Teensy and LORA-E5
Swapped RX and TX pins. Fixes #7
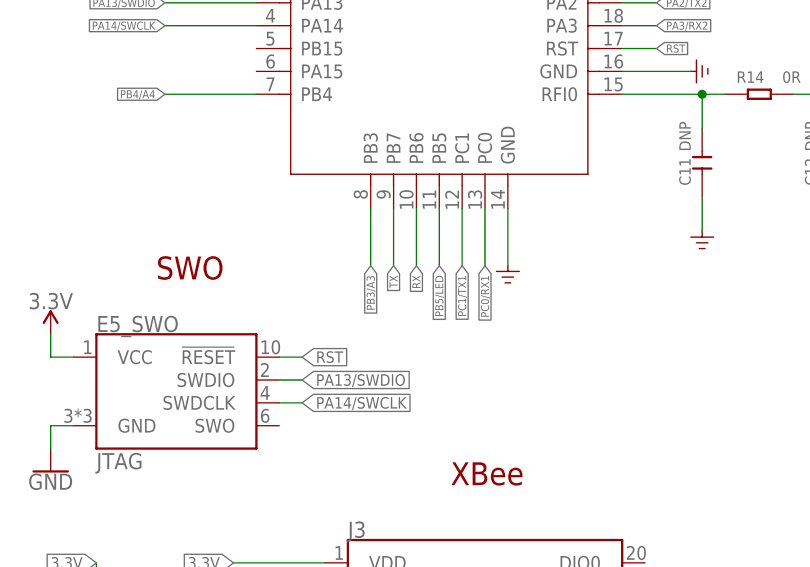
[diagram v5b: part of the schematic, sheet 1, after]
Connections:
- net RX: now also U7.PB6; no longer U7.PB7
- net TX: now also U7.PB7; no longer U7.PB6
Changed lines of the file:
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@@
-</segment>
-<segment>
-<pinref part="U7" gate="G$1" pin="PB6"/>
-<wire x1="284.48" y1="186.69" x2="284.48" y2="180.34" width="0.1524" layer="91" grouprefs="WIRELESS"/>
-<label x="284.48" y="180.34" size="0.889" layer="95" ratio="12" rot="R270" xref="yes" grouprefs="WIRELESS"/>
 </segment>
 <segment>
@@
 <wire x1="264.16" y1="142.24" x2="274.32" y2="142.24" width="0.1524" layer="91" grouprefs="WIRELESS"/>
 </segment>
+<segment>
+<pinref part="U7" gate="G$1" pin="PB7"/>
+<wire x1="281.94" y1="186.69" x2="281.94" y2="180.34" width="0.1524" layer="91" grouprefs="WIRELESS"/>
+<label x="281.94" y="180.34" size="0.889" layer="95" ratio="12" rot="R270" xref="yes" grouprefs="WIRELESS"/>
+</segment>
 </net>
 <net name="RX" class="2">
@@
 <label x="73.66" y="182.88" size="1.27" layer="95" xref="yes" grouprefs="MICROMOD"/>
 <pinref part="J7" gate="J1" pin="RX1"/>
-</segment>
-<segment>
-<pinref part="U7" gate="G$1" pin="PB7"/>
-<wire x1="281.94" y1="186.69" x2="281.94" y2="180.34" width="0.1524" layer="91" grouprefs="WIRELESS"/>
-<label x="281.94" y="180.34" size="0.889" layer="95" ratio="12" rot="R270" xref="yes" grouprefs="WIRELESS"/>
 </segment>
 <segment>
@@
 <wire x1="264.16" y1="144.78" x2="274.32" y2="144.78" width="0.1524" layer="91" grouprefs="WIRELESS"/>
 </segment>
+<segment>
+<pinref part="U7" gate="G$1" pin="PB6"/>
+<wire x1="284.48" y1="186.69" x2="284.48" y2="180.34" width="0.1524" layer="91" grouprefs="WIRELESS"/>
+<label x="284.48" y="180.34" size="0.889" layer="95" ratio="12" rot="R270" xref="yes" grouprefs="WIRELESS"/>
+</segment>
 </net>
